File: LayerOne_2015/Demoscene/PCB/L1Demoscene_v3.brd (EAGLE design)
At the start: 50 x 50 mm, 42 parts, among them IC2 REG1117, J1 CON_HEADER_1X02-PTH, J2 CON_HEADER_1X02-PTH, J3 CON_HEADER_2X04-PTH, U2 PIC24FXXXDAX06

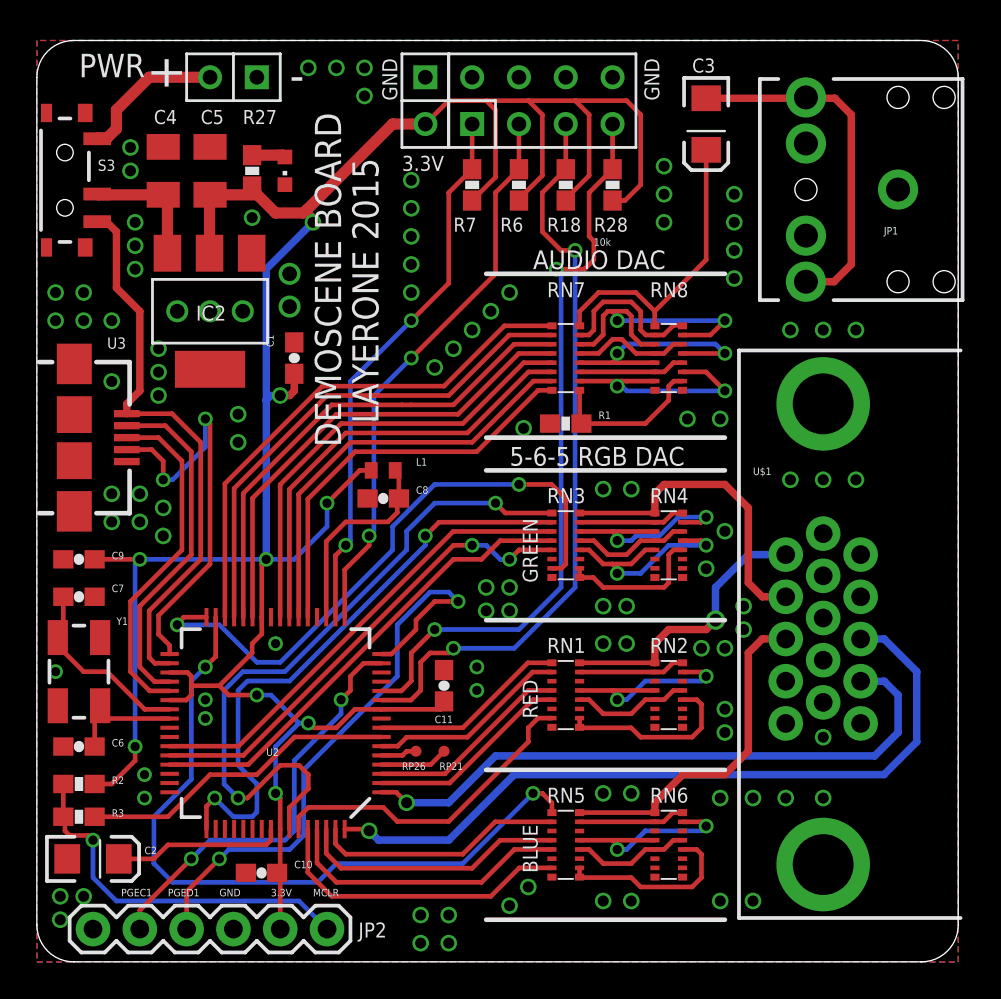
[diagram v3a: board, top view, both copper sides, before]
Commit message: Updated with L1 logo and a few fonts are blown up
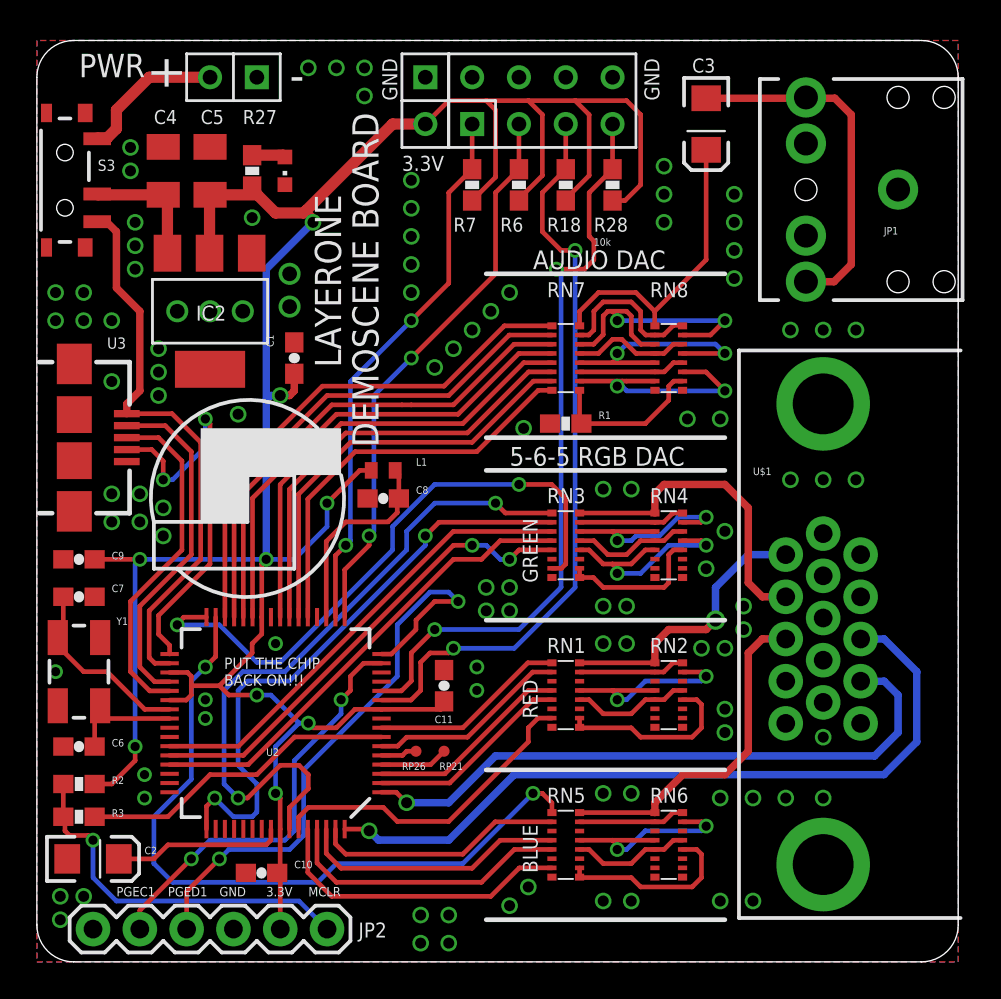
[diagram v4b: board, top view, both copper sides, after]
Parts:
- added U$2: (no value), STM32-PROX-L1:STM32-PROX_L1LOGO
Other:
- board text added: "LAYERONE"
- board text added: "PUT THE CHIP BACK ON!!!"
- board text removed: "LAYERONE 2015"
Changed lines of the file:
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@@
 <wire x1="2" y1="0" x2="48" y2="0" width="0" layer="20"/>
 <wire x1="48" y1="0" x2="50" y2="2" width="0" layer="20" curve="90"/>
-<text x="18.542" y="29.21" size="1.4224" layer="21" font="vector" ratio="12" rot="R90">LAYERONE 2015</text>
-<text x="16.51" y="27.94" size="1.4224" layer="21" font="vector" ratio="12" rot="R90">DEMOSCENE BOARD</text>
+<text x="16.51" y="32.258" size="1.4224" layer="21" font="vector" ratio="12" rot="R90">LAYERONE</text>
+<text x="18.542" y="27.94" size="1.4224" layer="21" font="vector" ratio="12" rot="R90">DEMOSCENE BOARD</text>
 <text x="7.874" y="47.244" size="1.9304" layer="21" rot="R90">+</text>
 <wire x1="37.338" y1="10.414" x2="24.384" y2="10.414" width="0.254" layer="25"/>
@@
 <text x="19.558" y="46.736" size="0.8128" layer="25" rot="R90">GND</text>
 <text x="33.782" y="46.736" size="0.8128" layer="25" rot="R90">GND</text>
-<text x="4.572" y="3.556" size="0.4064" layer="25">PGEC1</text>
-<text x="7.112" y="3.556" size="0.4064" layer="25">PGED1</text>
-<text x="9.906" y="3.556" size="0.4064" layer="25">GND</text>
-<text x="12.7" y="3.556" size="0.4064" layer="25">3.3V</text>
-<text x="14.986" y="3.556" size="0.4064" layer="25">MCLR</text>
+<text x="4.318" y="3.556" size="0.508" layer="25">PGEC1</text>
+<text x="7.112" y="3.556" size="0.508" layer="25">PGED1</text>
+<text x="9.906" y="3.556" size="0.508" layer="25">GND</text>
+<text x="12.446" y="3.556" size="0.508" layer="25">3.3V</text>
+<text x="14.732" y="3.556" size="0.508" layer="25">MCLR</text>
+<text x="10.16" y="14.986" size="0.6096" layer="25">PUT THE CHIP
+BACK ON!!!</text>
 </plain>
 <attributes>
@@
 <attribute name="NAME" x="21.844" y="10.414" size="0.4064" layer="25"/>
 </element>
+<element name="U$2" library="STM32-PROX-L1" package="STM32-PROX_L1LOGO" value="" x="11.43" y="25.146" rot="R90"/>
 </elements>
 <signals>
@@
 </board>
 </drawing>
+<compatibility>
+<note version="6.3" minversion="6.2.2" severity="warning">
+Since Version 6.2.2 text objects can contain more than one line,
+which will not be processed correctly with this version.
+</note>
+</compatibility>
 </eagle>
